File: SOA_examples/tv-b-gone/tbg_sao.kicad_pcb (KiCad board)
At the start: 2 copper layers, 38.3 x 25.2 mm, 9 parts, among them Q1 2N3904, U1 ATtiny85V-10PU

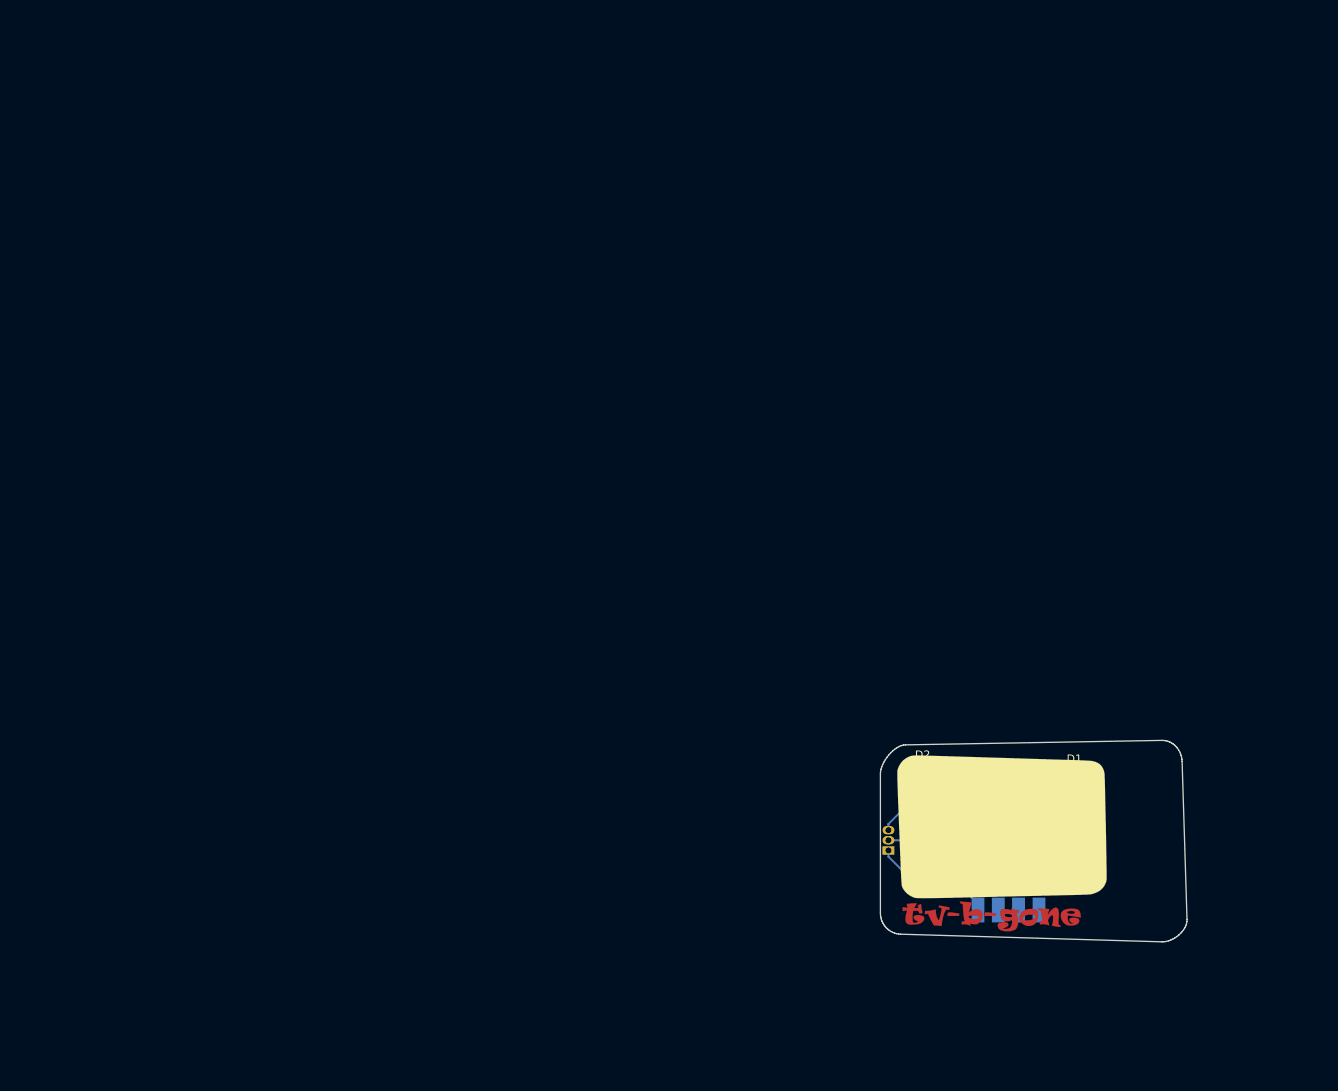
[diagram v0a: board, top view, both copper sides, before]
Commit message: Updated kicad stuff
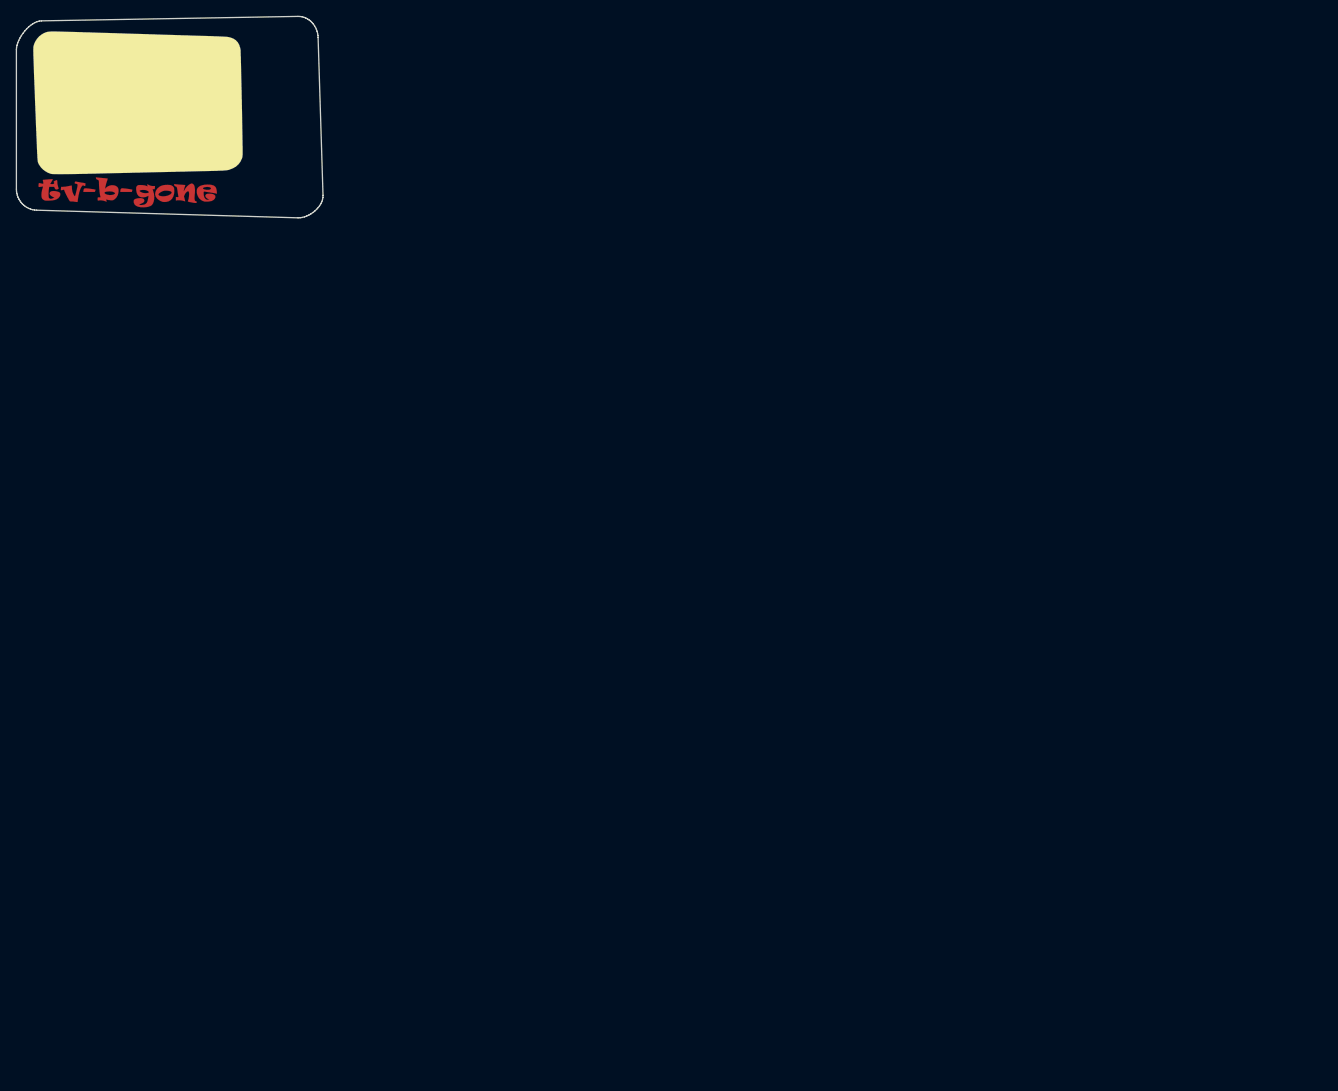
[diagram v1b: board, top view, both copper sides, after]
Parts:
- removed C1: C, Capacitor_SMD:C_1206_3216Metric_Pad1.42x1.75mm_HandSolder
- removed D1, D2: IR204A, LED_THT:LED_D5.0mm
- removed the G*** at (108.0, 90.5) (x2)
- removed the G*** at (0.00, 0.00)
- removed Q1: 2N3904, Package_TO_SOT_THT:TO-92_Inline
- removed R1: R, Resistor_SMD:R_1206_3216Metric_Pad1.42x1.75mm_HandSolder
- removed U1: ATtiny85V-10PU, Package_DIP:DIP-8_W8.89mm_SMDSocket_LongPads
- added G*** (x3): LOGO, LOGO, F.Cu at (0.00, 0.00)
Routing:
- net VCC: track 42.8 -> 0.00 mm
- net Net-(D1-Pad1): track 29.1 -> 0.00 mm
- net GND: track 15.2 -> 0.00 mm
- net Net-(Q1-Pad2): track 5.61 -> 0.00 mm
- net Net-(R1-Pad1): track 5.27 -> 0.00 mm

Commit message: Ready for the workshop
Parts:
- removed the G*** at (0.00, 0.00) (x3)
- added G*** (x2): LOGO, LOGO, F.Cu at (123.7, 102.6)
- added G***: LOGO, LOGO, F.Cu at (0.00, 0.00)

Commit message: WIP
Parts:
- removed the G*** at (123.7, 102.6) (x2)
- added C1: 100n, Capacitor_SMD:C_1206_3216Metric_Pad1.42x1.75mm_HandSolder, B.Cu at (115.4, 102.6)
- added C2: C, Capacitor_SMD:C_1206_3216Metric_Pad1.42x1.75mm_HandSolder, B.Cu at (105.9, 105.2)
- added C3: C, Capacitor_SMD:C_1206_3216Metric_Pad1.42x1.75mm_HandSolder, B.Cu at (105.4, 113.3)
- added D1: IR204A, LED_THT:LED_D5.0mm, F.Cu at (134.9, 104.9)
- added D2: IR204A, LED_THT:LED_D5.0mm, F.Cu at (134.9, 112.3)
- added G***: LOGO, LOGO, F.Cu at (123.7, 102.6)
- added G***: LOGO, LOGO, F.Cu at (123.4, 103.1)
- added Q1: 2N3904, Package_TO_SOT_THT:TO-92_Inline, B.Cu at (124.5, 104.9)
- added R1: 150R, Resistor_SMD:R_1206_3216Metric_Pad1.42x1.75mm_HandSolder, B.Cu at (125.5, 108.7)
- added SW1: SW_Push, Button_Switch_SMD:SW_Push_1P1T_NO_6x6mm_H9.5mm, F.Cu at (133.6, 120.9)
- added U1: ATtiny85V-10PU, Package_DIP:DIP-8_W8.89mm_SMDSocket_LongPads, B.Cu at (115.3, 109.5)
- added X1: Badgelife_sao_connector_v169bis, badgelife_sao_v169bis:Badgelife-SAOv169-SAO-2x3, F.Cu at (119.4, 119.1)
- added Y1: 8.0Mhz, Crystal:Crystal_AT310_D3.0mm_L10.0mm_Vertical, B.Cu at (104.1, 110.7)
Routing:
- net VCC: track 0.00 -> 38.3 mm
- net Net-(SW1-Pad1): track 0.00 -> 34.8 mm, vias 0 -> 1
- net Net-(D1-Pad1): track 0.00 -> 18.2 mm
- net Net-(C2-Pad1): track 0.00 -> 9.90 mm
- net Net-(C3-Pad1): track 0.00 -> 9.38 mm
- net GND: track 0.00 -> 8.04 mm, vias 0 -> 1
- net Net-(R1-Pad1): track 0.00 -> 7.01 mm
- net Net-(Q1-Pad2): track 0.00 -> 4.59 mm
- added copper zone on B.Cu, net GND
